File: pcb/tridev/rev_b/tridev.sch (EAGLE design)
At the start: 66 parts, among them J1 MICRO_USB_B_HIROSE_ZX62R-B-5P, J5 TC2030-JLINK-L, J6 TC2030-JLINK-L, U1 TRIPOINT-BREAKOUT, U2 NRF51822QF, U3 MAX8887EZK33+T, U4 FT232HQ, X1 EPSON-FA-128, X2 TXC-8Z-12MHZ

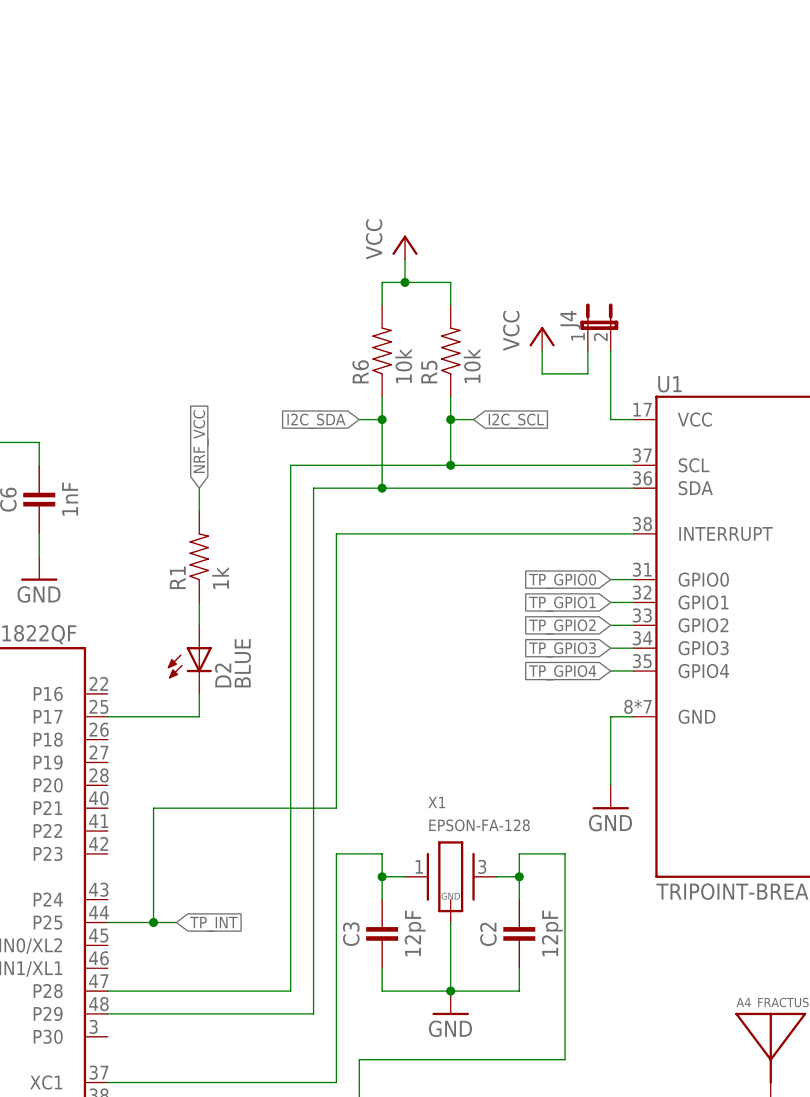
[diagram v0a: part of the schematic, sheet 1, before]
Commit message: update tridev with more jumpers
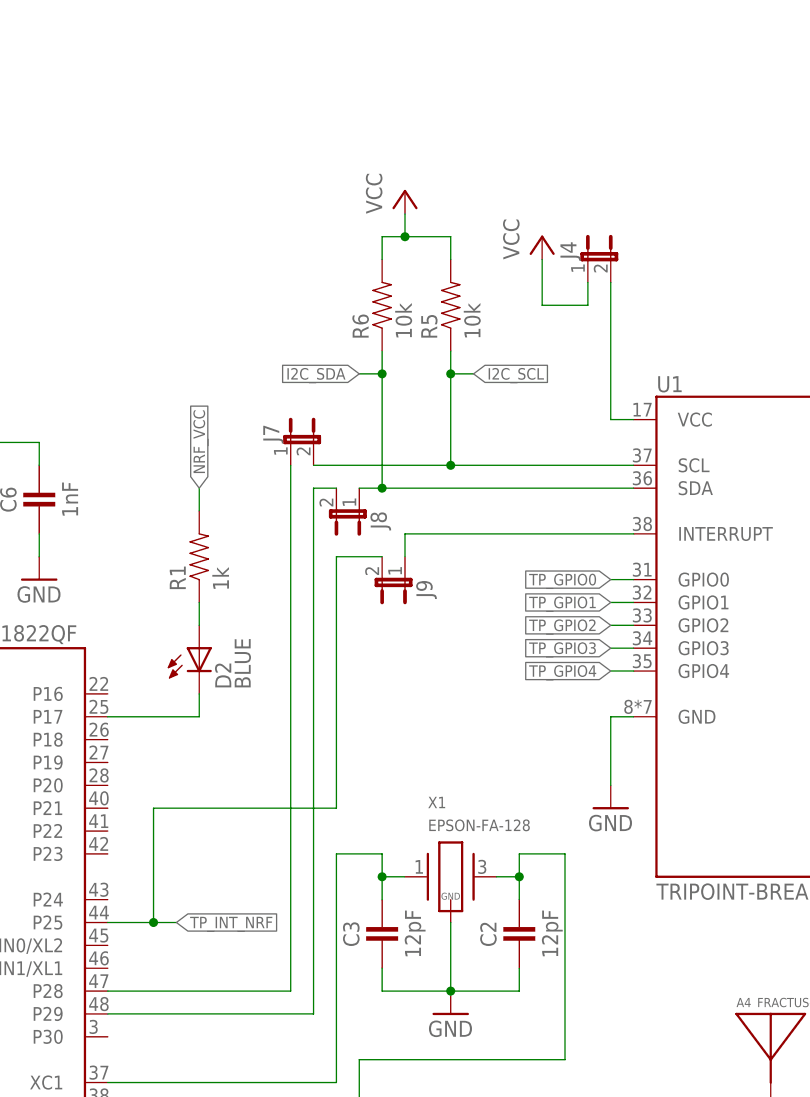
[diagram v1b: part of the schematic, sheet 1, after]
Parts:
- added J11, J12, J13, J7, J8, J9: (no value), SparkFun-Passives:JUMPER-2PTH
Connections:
- new net I2C_SCL_FTDI: J11.1, U4.ADBUS0
- new net I2C_SCL_NRF: J7.1, U2.P28
- new net I2C_SDA_FTDI: J12.2, U4.ADBUS1, U4.ADBUS2
- new net I2C_SDA_NRF: J8.2, U2.P29
- new net TP_INT_FTDI: J13.2, U4.ADBUS7
- new net TP_INT_NRF: J9.2, U2.P25
- net I2C_SCL: now also J11.2, J7.2; no longer U2.P28, U4.ADBUS0
- net I2C_SDA: now also J12.1, J8.1; no longer U2.P29, U4.ADBUS1, U4.ADBUS2
- net TP_INT: now also J13.1, J9.1; no longer U2.P25, U4.ADBUS7
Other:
- moved on the sheet: J4, R4, R5, R6
